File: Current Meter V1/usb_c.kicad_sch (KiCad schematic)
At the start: 3 parts, among them J601 USB_C_Receptacle_PowerOnly_6P

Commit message: microcontroller update
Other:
- moved on the sheet: R601, R602
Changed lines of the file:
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@@
 	(wire
 		(pts
-			(xy 152.4 90.17) (xy 154.94 90.17)
-		)
-		(stroke
-			(width 0)
-			(type default)
-		)
-	)
-	(wire
-		(pts
-			(xy 152.4 88.9) (xy 152.4 90.17)
+			(xy 152.4 91.44) (xy 154.94 91.44)
+		)
+		(stroke
+			(width 0)
+			(type default)
+		)
+	)
+	(wire
+		(pts
+			(xy 152.4 88.9) (xy 152.4 91.44)
 		)
 		(stroke
@@
 	(wire
 		(pts
-			(xy 162.56 85.09) (xy 162.56 83.82)
-		)
-		(stroke
-			(width 0)
-			(type default)
-		)
-	)
-	(wire
-		(pts
-			(xy 152.4 85.09) (xy 154.94 85.09)
+			(xy 152.4 83.82) (xy 154.94 83.82)
 		)
 		(stroke
@@
 	(wire
 		(pts
-			(xy 152.4 86.36) (xy 152.4 85.09)
-		)
-		(stroke
-			(width 0)
-			(type default)
-		)
-	)
-	(wire
-		(pts
-			(xy 162.56 90.17) (xy 167.64 90.17)
+			(xy 152.4 86.36) (xy 152.4 83.82)
+		)
+		(stroke
+			(width 0)
+			(type default)
+		)
+	)
+	(wire
+		(pts
+			(xy 162.56 91.44) (xy 167.64 91.44)
 		)
 		(stroke
@@
 	(symbol
 		(lib_id "Device:R_US")
-		(at 158.75 90.17 90)
+		(at 158.75 91.44 90)
 		(unit 1)
 		(exclude_from_sim no)
@@
 		(dnp no)
 		(property "Reference" "R602"
-			(at 158.75 92.964 90)
+			(at 158.75 94.234 90)
 			(effects
 				(font
@@
 		)
 		(property "Value" "5.1k Ohms"
-			(at 158.75 95.504 90)
-			(effects
-				(font
-					(size 1.27 1.27)
-				)
-			)
-		)
-		(property "Footprint" ""
-			(at 159.004 89.154 90)
+			(at 158.75 96.774 90)
+			(effects
+				(font
+					(size 1.27 1.27)
+				)
+			)
+		)
+		(property "Footprint" ""
+			(at 159.004 90.424 90)
 			(effects
 				(font
@@
 		)
 		(property "Datasheet" "~"
-			(at 158.75 90.17 0)
+			(at 158.75 91.44 0)
 			(effects
 				(font
@@
 		)
 		(property "Description" "Resistor, US symbol"
-			(at 158.75 90.17 0)
+			(at 158.75 91.44 0)
 			(effects
 				(font
@@
 	(symbol
 		(lib_id "power:GND")
-		(at 167.64 90.17 0)
+		(at 167.64 91.44 0)
 		(unit 1)
 		(exclude_from_sim no)
@@
 		(dnp no)
 		(property "Reference" "#PWR0605"
-			(at 167.64 96.52 0)
+			(at 167.64 97.79 0)
 			(effects
 				(font
@@
 		)
 		(property "Value" "GND"
-			(at 167.64 94.234 0)
-			(effects
-				(font
-					(size 1.27 1.27)
-				)
-			)
-		)
-		(property "Footprint" ""
-			(at 167.64 90.17 0)
+			(at 167.64 95.504 0)
+			(effects
+				(font
+					(size 1.27 1.27)
+				)
+			)
+		)
+		(property "Footprint" ""
+			(at 167.64 91.44 0)
 			(effects
 				(font
@@
 		)
 		(property "Datasheet" ""
-			(at 167.64 90.17 0)
+			(at 167.64 91.44 0)
 			(effects
 				(font
@@
 		)
 		(property "Description" "Power symbol creates a global label with name \"GND\" , ground"
-			(at 167.64 90.17 0)
+			(at 167.64 91.44 0)
 			(effects
 				(font
@@
 	(symbol
 		(lib_id "Device:R_US")
-		(at 158.75 85.09 90)
+		(at 158.75 83.82 90)
 		(unit 1)
 		(exclude_from_sim no)
@@
 		(fields_autoplaced yes)
 		(property "Reference" "R601"
-			(at 158.75 78.74 90)
+			(at 158.75 77.47 90)
 			(effects
 				(font
@@
 		)
 		(property "Value" "5.1k Ohms"
-			(at 158.75 81.28 90)
-			(effects
-				(font
-					(size 1.27 1.27)
-				)
-			)
-		)
-		(property "Footprint" ""
-			(at 159.004 84.074 90)
+			(at 158.75 80.01 90)
+			(effects
+				(font
+					(size 1.27 1.27)
+				)
+			)
+		)
+		(property "Footprint" ""
+			(at 159.004 82.804 90)
 			(effects
 				(font
@@
 		)
 		(property "Datasheet" "~"
-			(at 158.75 85.09 0)
+			(at 158.75 83.82 0)
 			(effects
 				(font
@@
 		)
 		(property "Description" "Resistor, US symbol"
-			(at 158.75 85.09 0)
-			(effects
-				(font
+			(at 158.75 83.82 0)
+			(effects
+				(font

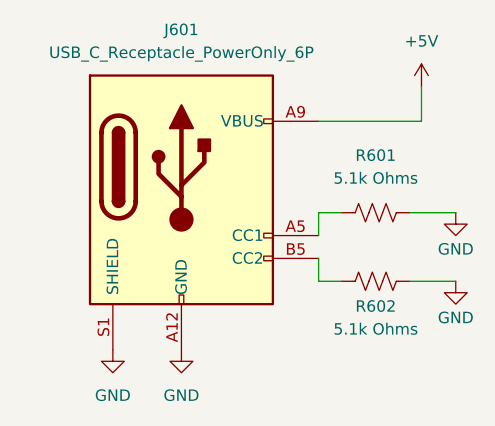
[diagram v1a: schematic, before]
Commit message: updated footprints
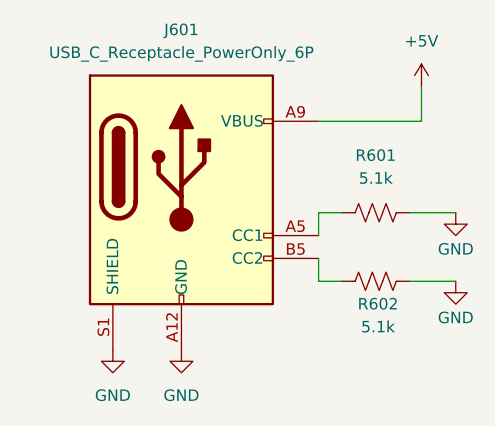
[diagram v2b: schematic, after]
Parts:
- removed R601, R602: 5.1k Ohms, symbol Device:R_US
- added R601, R602: 5.1k, Resistor_SMD:R_0805_2012Metric_Pad1.20x1.40mm_HandSolder, symbol bfr_resistors:RMCF0805FT5K10
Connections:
- net GND: now also R601.2, R602.2
- net at J601.B5 (CC2): now also R602.1
- net at J601.A5 (CC1): now also R601.1
